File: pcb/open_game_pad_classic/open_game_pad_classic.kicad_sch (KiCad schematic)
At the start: 44 parts, among them J1 COM-09032, J2 COM-09032, U1 MM74C923, U2 74HC4051, U3 74AHC1G00

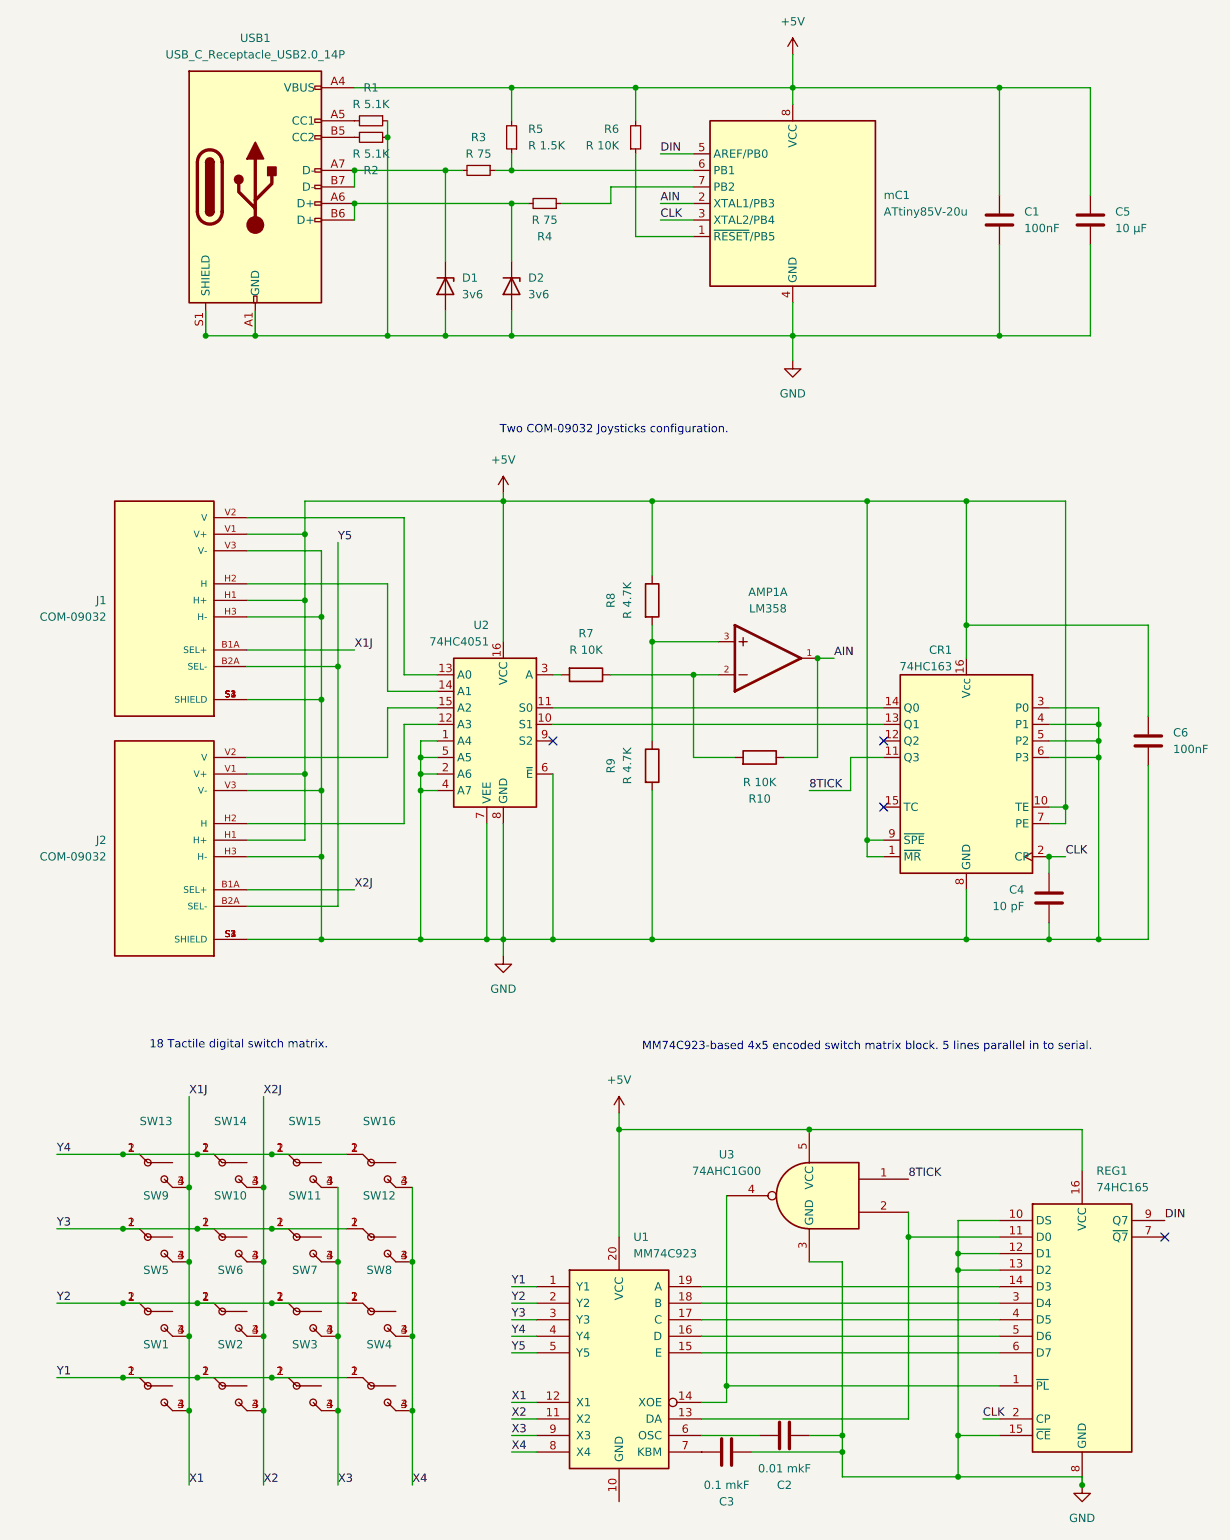
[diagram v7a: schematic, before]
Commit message: Removed the obsolete parts. Changed the logic completely to use one SIPO register. Using external counter to plex four analog and four digital inputs in one double 74hc4052.
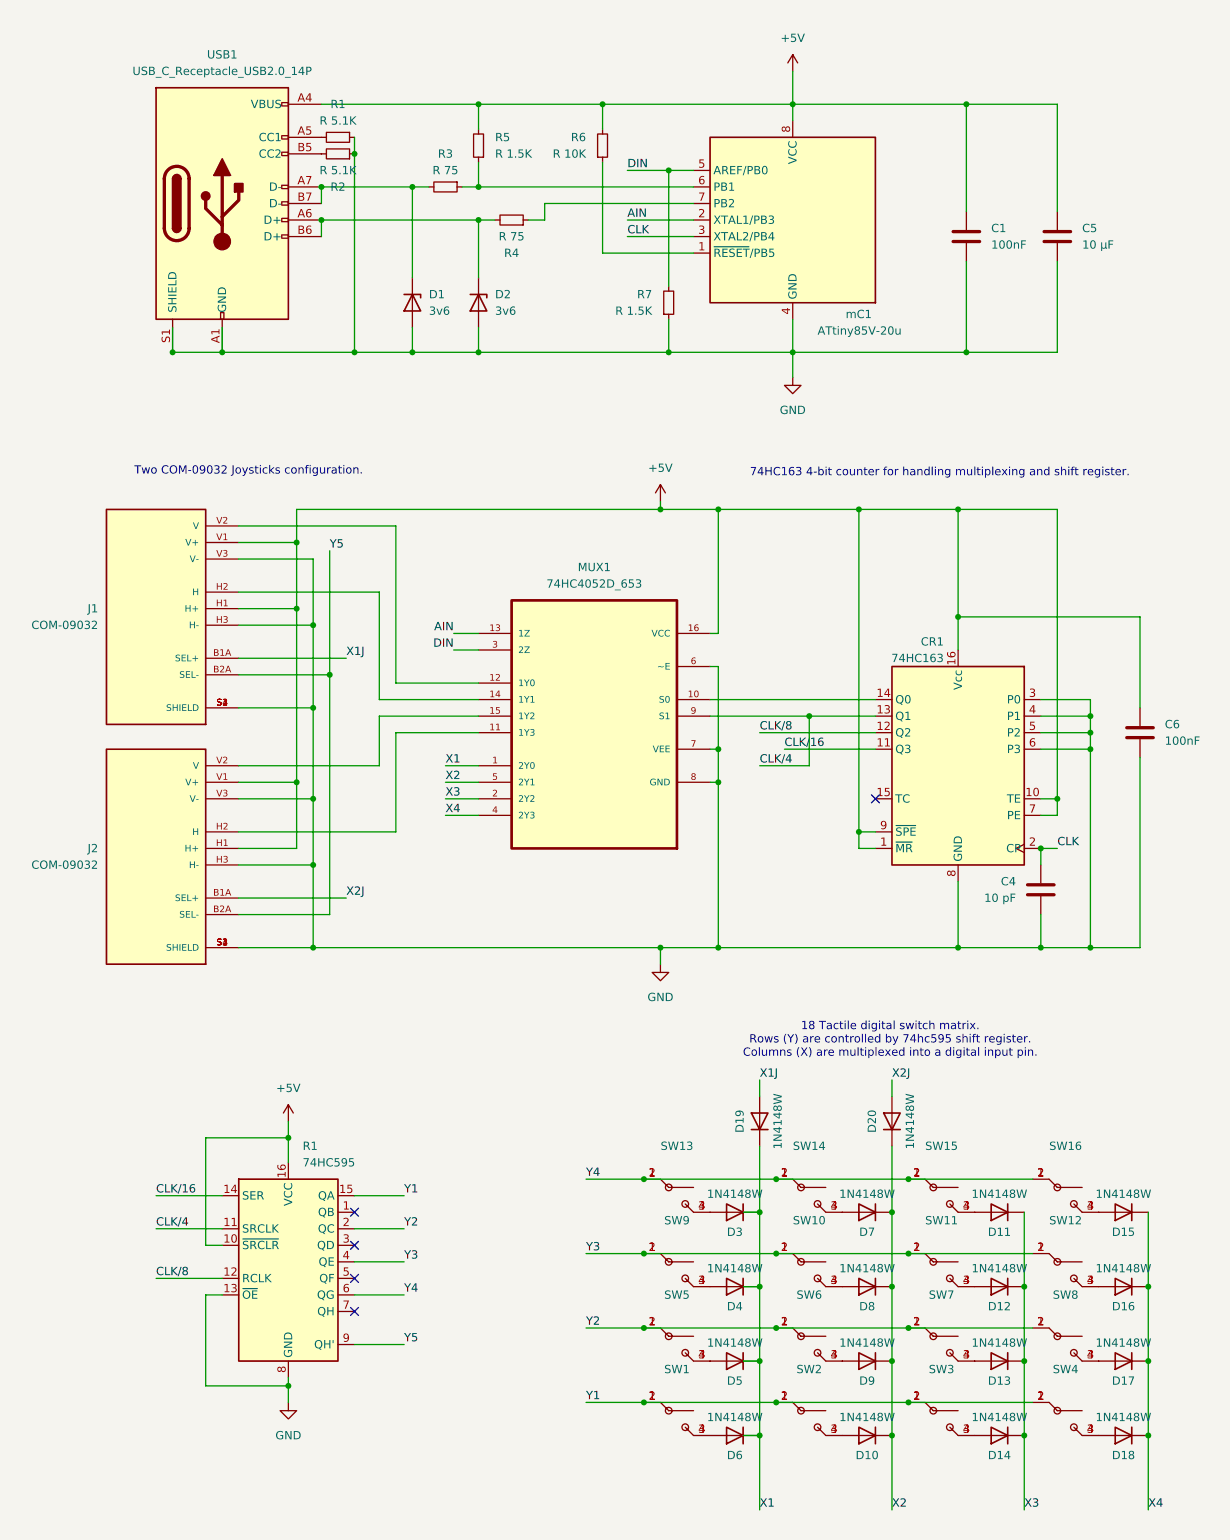
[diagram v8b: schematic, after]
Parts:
- removed AMP1: LM358, LM358:DIL8, symbol LM358:LM358
- removed C2: 0.01 mkF, Capacitor_SMD:C_0201_0603Metric, symbol Device:C
- removed C3: 0.1 mkF, Capacitor_SMD:C_0201_0603Metric, symbol Device:C
- removed R10: R 10K, Resistor_SMD:R_0805_2012Metric, symbol Device:R
- removed R7: R 10K, Resistor_SMD:R_0402_1005Metric, symbol Device:R
- removed R8, R9: R 4.7K, Resistor_SMD:R_0402_1005Metric, symbol Device:R
- removed REG1: 74HC165, Package_SO:SOIC-16_3.9x9.9mm_P1.27mm, symbol 74xx:74HC165
- removed U1: MM74C923, Package_SO:SOIC-20W_7.5x12.8mm_P1.27mm, symbol 74xx:MM74C923
- removed U2: 74HC4051, Package_SO:TSSOP-16_4.4x5mm_P0.65mm, symbol 74xx:74HC4051
- removed U3: 74AHC1G00, Package_TO_SOT_SMD:SOT-23-5, symbol 74xGxx:74AHC1G00
- added D10, D11, D12, D13, D14, D15, D16, D17, D18, D19, D20, D3, D4, D5, D6, D7, D8, D9: 1N4148W, Diode_SMD:D_SOD-123, symbol Diode:1N4148W
- added MUX1: 74HC4052D_653, 74HC4052D_653:SOIC127P600X175-16N, symbol 74HC4052D_653_NIX:74HC4052D_653
- added R1: 74HC595, symbol 74xx:74HC595
- added R7: R 1.5K, Resistor_SMD:R_0603_1608Metric, symbol Device:R_Small
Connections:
- net +5V: now also MUX1.16 (VCC), R1.10 (~{SRCLR}), R1.16 (VCC)
- net AIN: now also MUX1.13 (1Z)
- net DIN: now also MUX1.3 (2Z), R7.2
- net GND: now also MUX1.6 (~E), MUX1.7 (VEE), MUX1.8 (GND), R1.13 (~{OE}), R1.8 (GND), R7.1
- net X1: now also D19.1 (K), D3.1 (K), D4.1 (K), D5.1 (K), D6.1 (K), MUX1.1 (2Y0); no longer J1.B1A (SEL+), SW1.3 (B), SW1.4 (B), SW13.3 (B), SW13.4 (B), SW5.3 (B), SW5.4 (B), SW9.3 (B), SW9.4 (B)
- net X2: now also D10.1 (K), D20.1 (K), D7.1 (K), D8.1 (K), D9.1 (K), MUX1.5 (2Y1); no longer J2.B1A (SEL+), SW10.3 (B), SW10.4 (B), SW14.3 (B), SW14.4 (B), SW2.3 (B), SW2.4 (B), SW6.3 (B), SW6.4 (B)
- net X3: now also D11.1 (K), D12.1 (K), D13.1 (K), D14.1 (K), MUX1.2 (2Y2); no longer SW11.3 (B), SW11.4 (B), SW15.3 (B), SW15.4 (B), SW3.3 (B), SW3.4 (B), SW7.3 (B), SW7.4 (B)
- net X4: now also D15.1 (K), D16.1 (K), D17.1 (K), D18.1 (K), MUX1.4 (2Y3); no longer SW12.3 (B), SW12.4 (B), SW16.3 (B), SW16.4 (B), SW4.3 (B), SW4.4 (B), SW8.3 (B), SW8.4 (B)
- net Y1: now also R1.15 (QA)
- net Y2: now also R1.2 (QC)
- net Y3: now also R1.4 (QE)
- net Y4: now also R1.6 (QG)
- net Y5: now also R1.9 (QH')
- net CLK/4: now reaches CR1.13 (Q1)
- net CLK/4: now also MUX1.9 (S1), R1.11 (SRCLK)
- net at CR1.14 (Q0): now also MUX1.10 (S0)
- net at J2.H2 (H): now also MUX1.11 (1Y3)
- net at J1.V2 (V): now also MUX1.12 (1Y0)
- net at J1.H2 (H): now also MUX1.14 (1Y1)
- net at J2.V2 (V): now also MUX1.15 (1Y2)
- net CLK/8: now reaches CR1.12 (Q2)
- net CLK/8: now also R1.12 (RCLK)
- net 8TICK renamed CLK/16
- net CLK/16: now also R1.14 (SER)
- new net: D11.2 (A), SW15.3 (B), SW15.4 (B)
- new net: D10.2 (A), SW2.3 (B), SW2.4 (B)
- new net: D3.2 (A), SW13.3 (B), SW13.4 (B)
- new net: D14.2 (A), SW3.3 (B), SW3.4 (B)
- new net: D15.2 (A), SW16.3 (B), SW16.4 (B)
- new net: D8.2 (A), SW10.3 (B), SW10.4 (B)
- new net: D18.2 (A), SW4.3 (B), SW4.4 (B)
- new net: D5.2 (A), SW5.3 (B), SW5.4 (B)
- new net: D12.2 (A), SW11.3 (B), SW11.4 (B)
- new net: D13.2 (A), SW7.3 (B), SW7.4 (B)
- new net: D9.2 (A), SW6.3 (B), SW6.4 (B)
- new net: D17.2 (A), SW8.3 (B), SW8.4 (B)
- new net: D4.2 (A), SW9.3 (B), SW9.4 (B)
- new net: D16.2 (A), SW12.3 (B), SW12.4 (B)
- new net: D6.2 (A), SW1.3 (B), SW1.4 (B)
- new net: D7.2 (A), SW14.3 (B), SW14.4 (B)
- new net X1J: D19.2 (A), J1.B1A (SEL+)
- new net X2J: D20.2 (A), J2.B1A (SEL+)
- no-connect marks 4 -> 5
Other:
- note added: "18 Tactile digital switch matrix. Rows (Y) are controlled by 74hc595 shift register. Columns (X) are multiplexed into a digital input pin."
- note added: "74HC163 4-bit counter for handling multiplexing and shift register."
- note removed: "18 Tactile digital switch matrix."
- note removed: "MM74C923-based 4x5 encoded switch matrix block. 5 lines parallel in to serial."
- moved on the sheet: C1, C4, C5, C6, CR1, D1, D2, J1, J2, R1, R2, R3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
